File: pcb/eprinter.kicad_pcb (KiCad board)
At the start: 4 copper layers, 28 x 70 mm, 55 parts, among them J1 USB_C_Receptacle_USB2.0_16P, J2 AFC07-S24FCC-00, J3 Conn_01x02_Pin, Q1 Si2301, Q2 BSS138, SW1 SW_PUSH, SW2 SW_PUSH, U1 ESP32-C3-WROOM-02, U2 LM3480-5.0, U3 LM66100DCK, U4 MIC841HYC5, U5 XC6220B331MR

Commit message: Finish PCB v1
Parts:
- R16: value 3M -> 2M
- R17: value 430k -> 330k
- R18: value 1.5M -> 1M

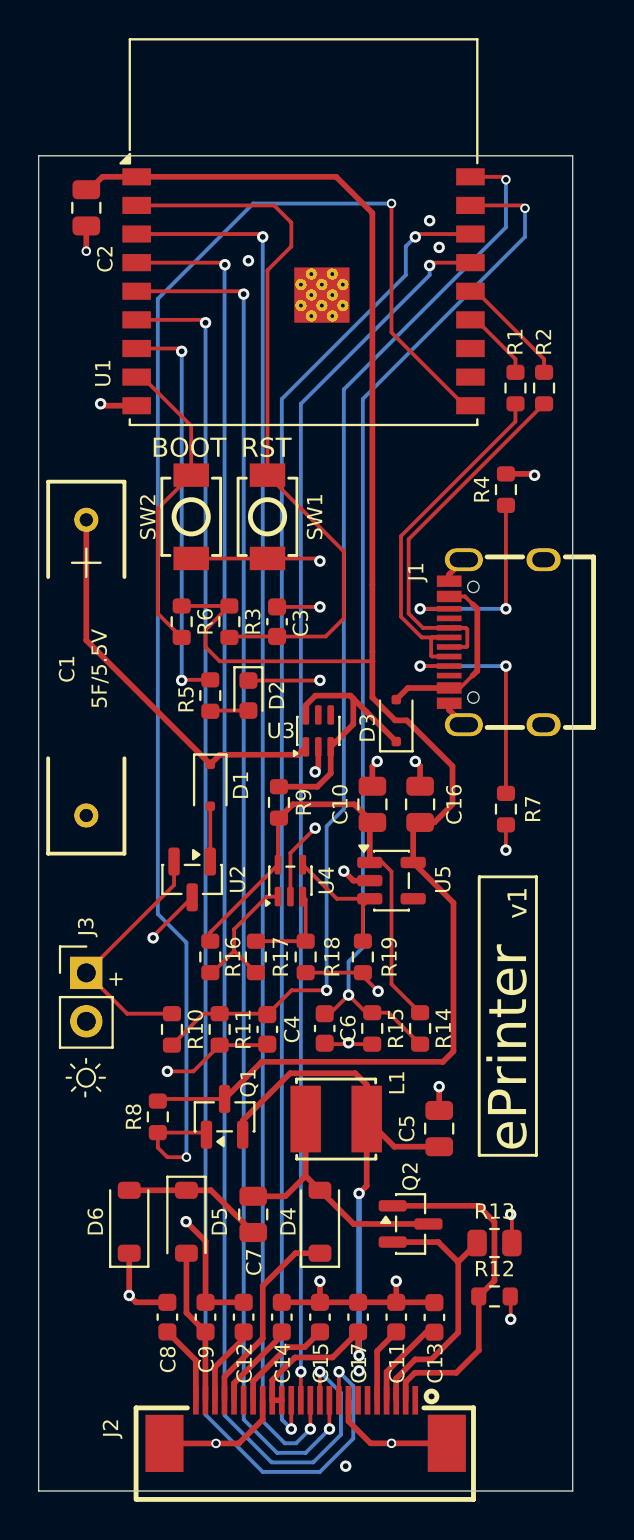
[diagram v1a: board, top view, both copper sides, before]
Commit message: Switch to buck-boost converter to utilize more super cap capacity
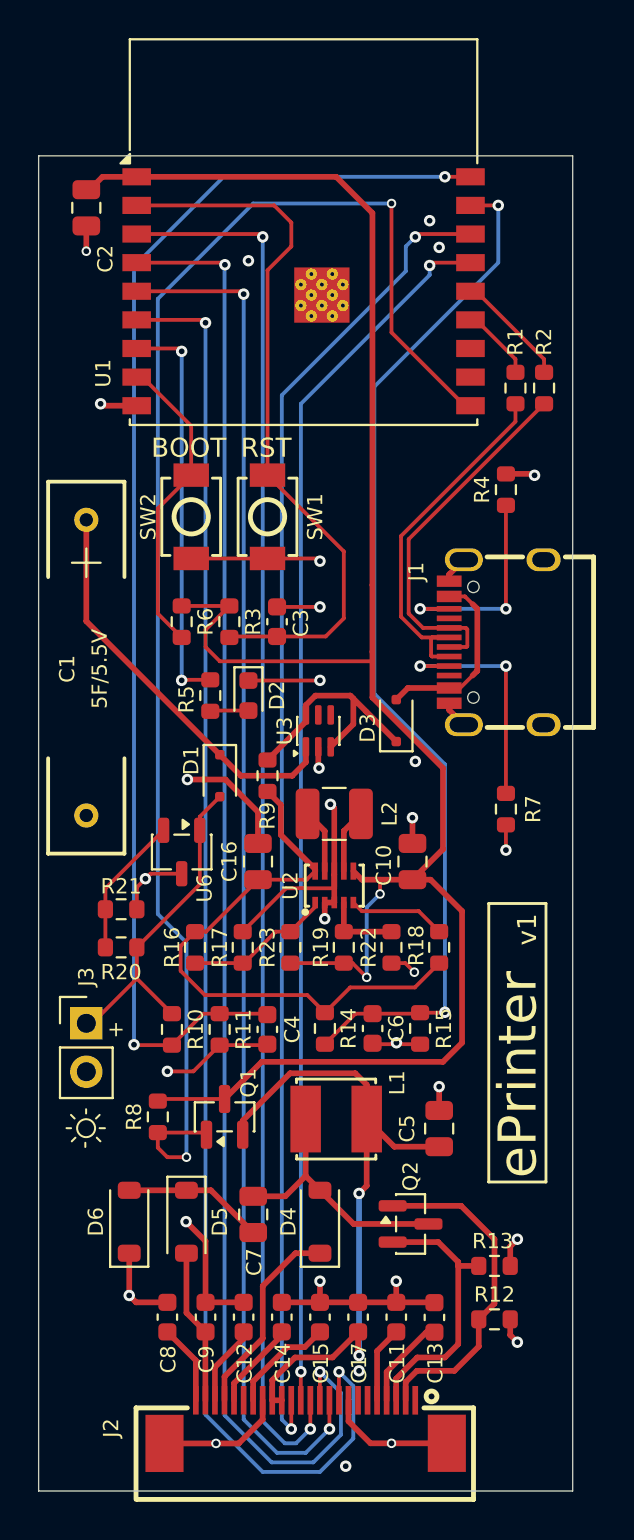
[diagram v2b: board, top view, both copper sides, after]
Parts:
- removed U4: MIC841HYC5, Package_TO_SOT_SMD:SOT-353_SC-70-5
- removed U5: XC6220B331MR, Package_TO_SOT_SMD:SOT-23-5
- added L2: 0.47u, Inductor_SMD:L_1210_3225Metric, F.Cu at (161.0, 82.5)
- added R20: 510k, Resistor_SMD:R_0603_1608Metric, F.Cu at (149.8, 89.5)
- added R21: 510k, Resistor_SMD:R_0603_1608Metric, F.Cu at (149.8, 87.5)
- added R22: 91k, Resistor_SMD:R_0603_1608Metric, F.Cu at (164.0, 89.5)
- added R23: 4.7M, Resistor_SMD:R_0603_1608Metric, F.Cu at (158.7, 89.5)
- added U6: ATL431BIDBZR, Package_TO_SOT_SMD:SOT-23-3, F.Cu at (153.0, 84.5)
- C10: value 10u -> 22u
- R13: footprint Resistor_SMD:R_0805_2012Metric -> Resistor_SMD:R_0603_1608Metric
- R16: value 2M -> 1M
- R17: value 330k -> 680k
- R18: value 1M -> 4.7M
- R19: value 4.7M -> 510k
- U2: value LM3480-5.0 -> TPS63802DLAR; footprint Package_TO_SOT_SMD:SOT-23 -> eprinter:VSON-10_L3.0-W2.0-P0.50-TL
- moved C16 9.01 mm to (157.0, 85.0)
- moved U2 7.46 mm to (161.0, 86.3), turned to 90 degrees
- moved R18 7.02 mm to (166.5, 89.5), turned to 90 degrees
- moved R14 4.99 mm to (160.5, 93.8)
- moved C10 3.66 mm to (165.1, 85.0)
- moved J3 2.64 mm to (148.0, 93.5)
- moved C6 2.51 mm to (163.0, 93.8)
- moved R15 2.51 mm to (165.5, 93.8)
- moved R9 1.52 mm to (157.5, 80.5)
- moved R12 1.20 mm to (169.4, 109.0)
- moved R13 1.20 mm to (169.4, 106.2)
- moved R19 1.12 mm to (161.5, 89.5)
- moved R16 0.94 mm to (153.7, 89.5)
- moved R17 0.85 mm to (156.2, 89.5)
- moved D1 0.71 mm to (155.0, 80.5)
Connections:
- C10 pad 1: /VIN -> +3V3
- C16 pad 1: +3V3 -> /VIN
- D1 pad 2: Net-(D1-A) -> /SOLAR+
- R16 pad 2: Net-(U4-HTH) -> Net-(U2-EN)
- R17 pad 1: Net-(U4-HTH) -> Net-(U2-EN)
- R17 pad 2: Net-(U4-LTH) -> GND
- R18 pad 1: Net-(U4-LTH) -> /VIN
- R18 pad 2: GND -> Net-(U2-PG)
- R19 pad 1: GND -> +3V3
- R19 pad 2: Net-(U4-OUT) -> Net-(U2-FB)
- U2 pad 1: Net-(D1-A) -> Net-(U2-EN)
- U2 pad 2: /SOLAR+ -> GND
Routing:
- net +3V3: track 95.3 -> 108.1 mm, vias 0 -> 2
- net /SOLAR_V: track 57.7 -> 68.1 mm
- net GND: track 86.3 -> 95.1 mm, vias 30 -> 31
- net Net-(U2-EN): track 0.00 -> 7.75 mm
- net Net-(U4-HTH): track 7.48 -> 0.00 mm
- net Net-(U6-REF): track 0.00 -> 7.40 mm
- net Net-(U4-OUT): track 6.63 -> 0.00 mm
- net /VIN: track 25.0 -> 30.7 mm
- net Net-(U2-PG): track 0.00 -> 5.13 mm
- net Net-(U4-LTH): track 5.01 -> 0.00 mm
- net /SOLAR+: track 13.1 -> 17.6 mm
- net Net-(U2-FB): track 0.00 -> 4.03 mm
- net Net-(U2-L1): track 0.00 -> 3.37 mm
- net Net-(U2-L2): track 0.00 -> 3.37 mm
- net Net-(D1-A): track 2.90 -> 0.00 mm
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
